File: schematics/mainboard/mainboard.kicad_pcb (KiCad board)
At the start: 4 copper layers, 92 x 166.8 mm, 75 parts, among them J1 SD_Card_Receptacle, J2 Conn_02x20_Odd_Even_MountingP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, J3 USB_C_Receptacle_USB2.0_16P, J6 Conn_01x12, P1 1-1473005-4, U1 AMS1117-3.3, U2 AMS1117-3.3, U3 MAX3421EETJ_T, U5 BQ24040DSQR, U6 TPS63002, U8 MAX9715xTE+, U9 AMS1117-3.3, Y1 12MHz

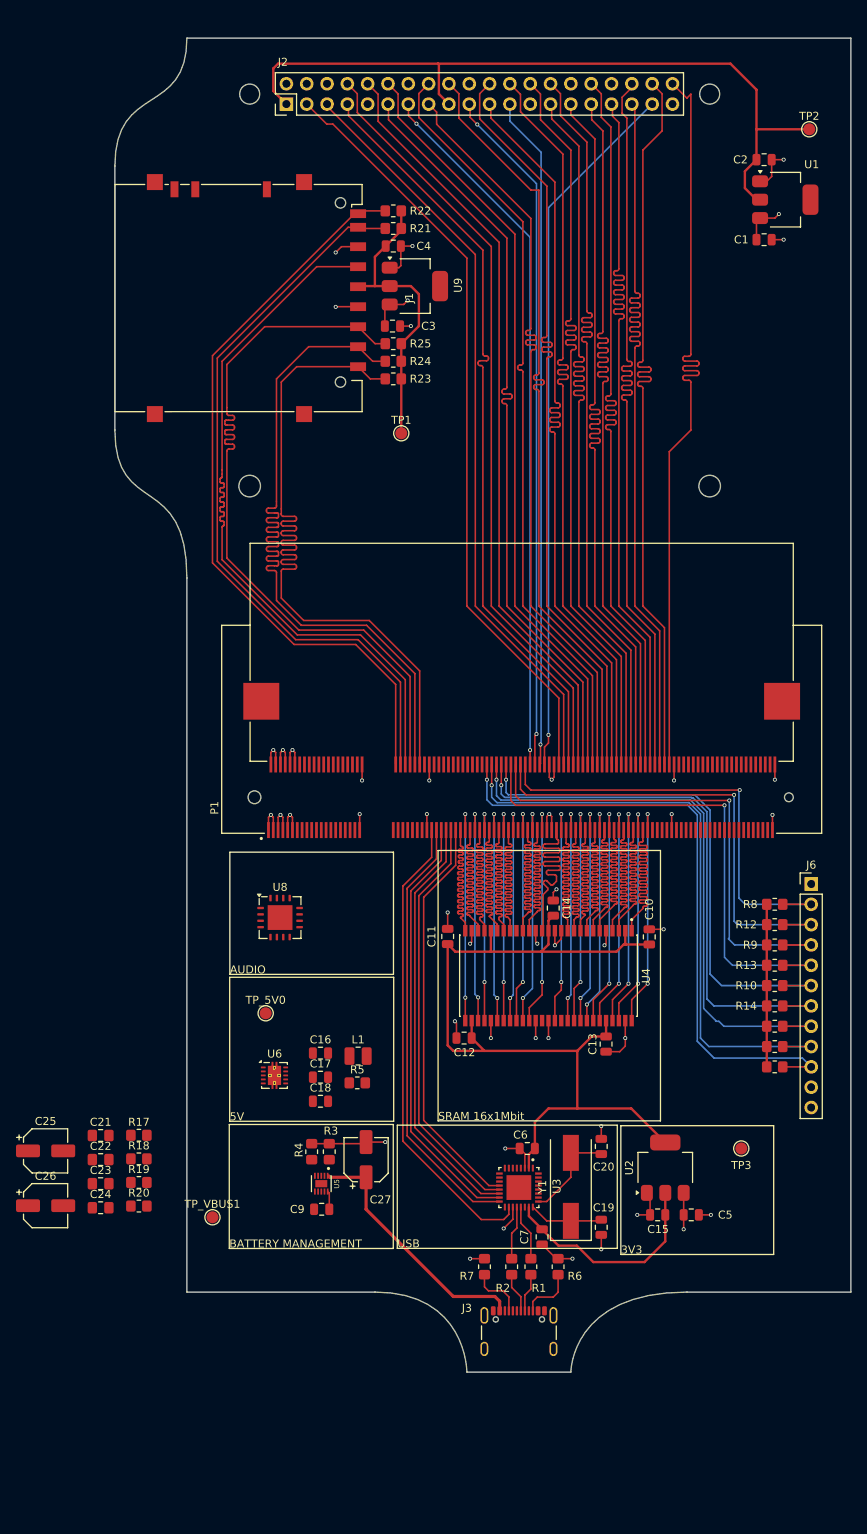
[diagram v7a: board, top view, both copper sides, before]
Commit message: Mainboard schematics, audio system and power traces.
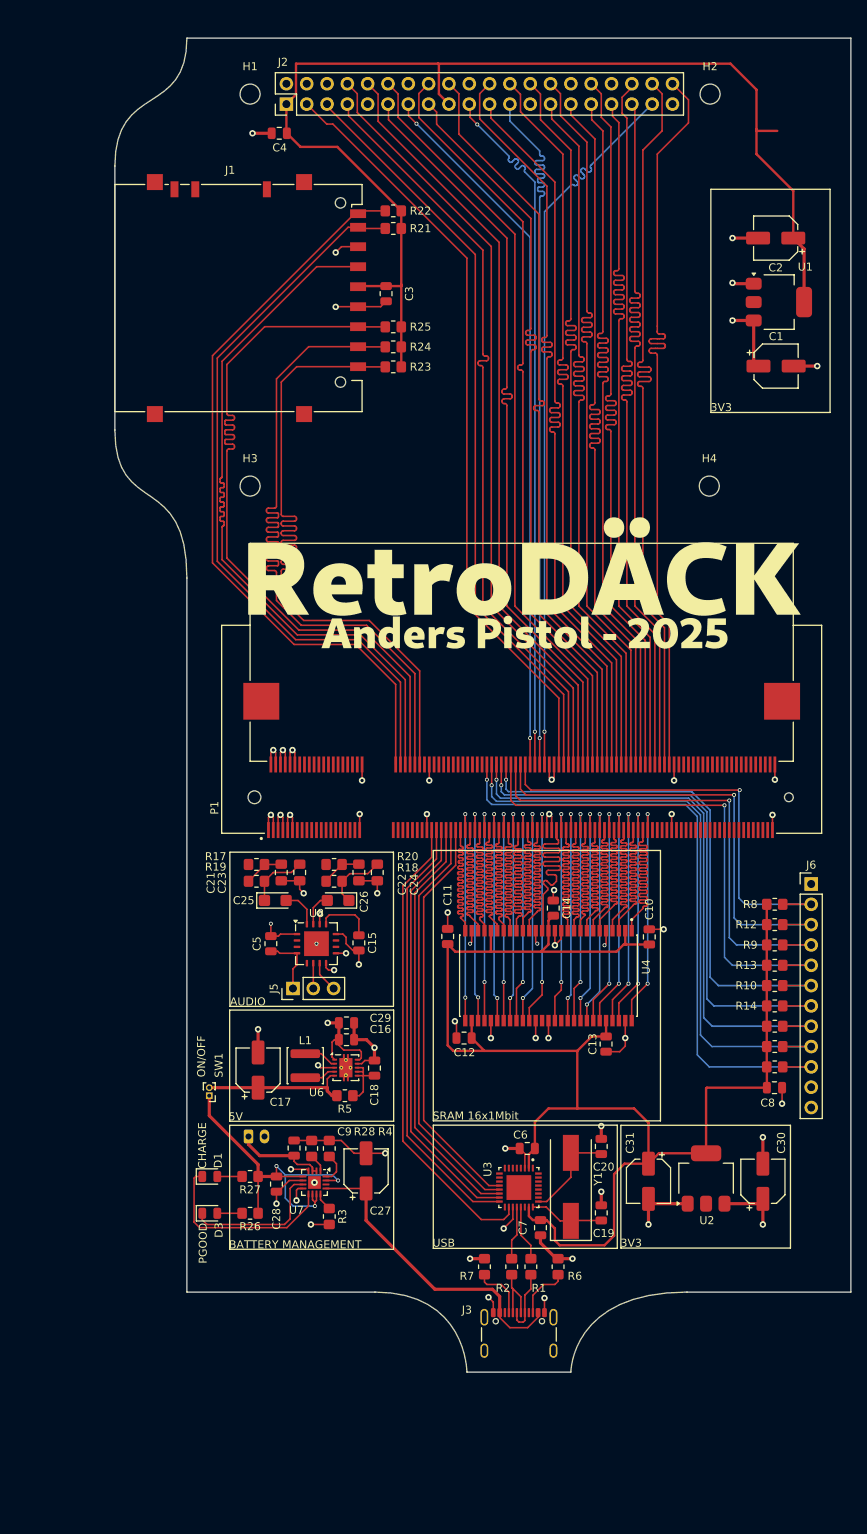
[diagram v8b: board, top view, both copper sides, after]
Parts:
- removed REF** (x2): MountingHole_2.7mm, MountingHole:MountingHole_2.7mm
- removed REF** (x2): MountingHole_2.5mm, MountingHole:MountingHole_2.5mm
- removed TP1: TP_3V3_SD, TestPoint:TestPoint_Pad_D1.5mm
- removed TP2: TP_3V3_LCD, TestPoint:TestPoint_Pad_D1.5mm
- removed TP3: TP_3V3, TestPoint:TestPoint_Pad_D1.5mm
- removed TP_5V0: TP_5V0, TestPoint:TestPoint_Pad_D1.5mm
- removed TP_VBUS1: TP_VBUS, TestPoint:TestPoint_Pad_D1.5mm
- removed U5: BQ24040DSQR, BQ24040DSQR:SON40P200X200X80-11N
- removed U9: AMS1117-3.3, Package_TO_SOT_SMD:SOT-223-3_TabPin2
- added C28: 10uF, Capacitor_SMD:C_0805_2012Metric, F.Cu at (126.2, 243.2)
- added C29: 10uF, Capacitor_SMD:C_0805_2012Metric, F.Cu at (134.9, 223.1)
- added C30: 10uF, Capacitor_SMD:CP_Elec_5x5.3, F.Cu at (187.0, 242.9)
- added C31: 22uF, Capacitor_SMD:CP_Elec_5x5.3, F.Cu at (172.7, 242.9)
- added C8: 1uF, Capacitor_SMD:C_0805_2012Metric, F.Cu at (188.4, 231.2)
- added D1: LED, LED_SMD:LED_0805_2012Metric, F.Cu at (117.9, 242.3)
- added D3: LED, LED_SMD:LED_0805_2012Metric, F.Cu at (117.9, 246.9)
- added H1: MountingHole, MountingHole:MountingHole_2.5mm, F.Cu at (122.9, 107.0)
- added H2: MountingHole, MountingHole:MountingHole_2.5mm, F.Cu at (180.4, 107.0)
- added H3: MountingHole, MountingHole:MountingHole_2.5mm, F.Cu at (122.9, 156.0)
- added H4: MountingHole, MountingHole:MountingHole_2.5mm, F.Cu at (180.3, 156.0)
- added J4: Conn_01x02, Connector_JST:JST_PH_S2B-PH-K_1x02_P2.00mm_Horizontal, B.Cu at (122.7, 237.3)
- added J5: Conn_01x03_Pin, Connector_PinHeader_2.54mm:PinHeader_1x03_P2.54mm_Vertical, F.Cu at (128.3, 218.8)
- added R26: 1k, Resistor_SMD:R_0805_2012Metric_Pad1.20x1.40mm_HandSolder, F.Cu at (122.9, 246.9)
- added R27: 1k, Resistor_SMD:R_0805_2012Metric_Pad1.20x1.40mm_HandSolder, F.Cu at (122.9, 242.3)
- added R28: 10k, Resistor_SMD:R_0805_2012Metric_Pad1.20x1.40mm_HandSolder, F.Cu at (130.6, 238.8)
- added SW1: SW_SPST, Connector_PinHeader_1.00mm:PinHeader_1x02_P1.00mm_Vertical, F.Cu at (117.8, 232.2)
- added U7: BQ24072RGT, Package_DFN_QFN:VQFN-16-1EP_3x3mm_P0.5mm_EP1.6x1.6mm, F.Cu at (130.9, 243.1)
- C1: value C -> 10uF; footprint Capacitor_SMD:C_0805_2012Metric -> Capacitor_SMD:CP_Elec_5x5.3
- C10, C11, C12, C13, C14, C15, C3, C4, C5, C6: value C -> 1uF
- C16: value 1u -> 10uF
- C17: value 10u -> 10uF; footprint Capacitor_SMD:C_0805_2012Metric -> Capacitor_SMD:CP_Elec_5x5.3
- C2: value C -> 22uF; footprint Capacitor_SMD:C_0805_2012Metric -> Capacitor_SMD:CP_Elec_5x5.3
- C25, C26: value 100uF -> 47uF; footprint Capacitor_SMD:CP_Elec_5x5.3 -> Capacitor_Tantalum_SMD:CP_EIA-3216-18_Kemet-A
- C7: value 1u -> 1uF
- C9: value 1u -> 4.7uF
- L1: value L -> 2.2uH; footprint Inductor_SMD:L_1008_2520Metric -> Inductor_SMD:L_APV_ANR4012
- R3: value 540 -> 1.18k
- R4: value 2k -> 1.13k
- moved C5 62.5 mm to (125.5, 213.2), turned to -90 degrees
- moved C24 54.3 mm to (138.8, 204.3), turned to 90 degrees
- moved C26 52.8 mm to (133.9, 207.8), turned to 180 degrees
- moved C15 50.5 mm to (136.5, 213.1), turned to -90 degrees
- moved C22 48.3 mm to (136.5, 204.3), turned to 90 degrees
- moved R20 47.4 mm to (133.4, 205.4)
- moved C23 46.2 mm to (129.1, 204.3), turned to -90 degrees
- moved R18 44.2 mm to (133.4, 203.3)
- moved C25 42.5 mm to (126.1, 207.8)
- moved R19 40.4 mm to (123.7, 205.4)
- moved C21 39.9 mm to (126.8, 204.3), turned to -90 degrees
- moved R17 36.9 mm to (123.7, 203.3)
- moved C4 20.0 mm to (126.5, 111.9), turned to 0 degrees
- moved C1 15.9 mm to (188.7, 141.0), turned to 0 degrees
- moved U1 12.8 mm to (189.0, 133.0)
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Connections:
- C1 pad 1: GND -> 5V0
- C1 pad 2: 5V0 -> GND
- C15 pad 1: GND -> Net-(U8-BIAS)
- C15 pad 2: 3V3 -> GND
- C17 pad 1: GND -> SYS_LOAD
- C17 pad 2: SYS_LOAD -> GND
- C2 pad 1: GND -> 3V3_LCD
- C2 pad 2: 3V3_LCD -> GND
- C21 pad 2: Net-(C21-Pad2) -> GND
- C22 pad 1: Net-(C21-Pad2) -> GND
- C23 pad 2: Net-(C21-Pad2) -> GND
- C24 pad 1: Net-(C21-Pad2) -> GND
- C3 pad 2: 5V0 -> 3V3_LCD
- C4 pad 2: 3V3_SD -> 3V3_LCD
- J1 pad 4: 3V3_SD -> 3V3_LCD
- R21 pad 2: 3V3_SD -> 3V3_LCD
- R22 pad 2: 3V3_SD -> 3V3_LCD
- R23 pad 2: 3V3_SD -> 3V3_LCD
- R24 pad 2: 3V3_SD -> 3V3_LCD
- R25 pad 2: 3V3_SD -> 3V3_LCD
- R3 pad 1: GND -> Net-(U7-ILIM)
- R3 pad 2: Net-(U5-ISET) -> GND
- R4 pad 1: GND -> Net-(U7-ISET)
- R4 pad 2: Net-(U5-PRETERM) -> GND
- U6 pad 10: unconnected-(U6-FB-Pad10) -> 5V0
- U8 pad 10: unconnected-(U8-OUTR--Pad10) -> Net-(U8-OUTR-)
- U8 pad 11: unconnected-(U8-OUTR+-Pad11) -> Net-(U8-OUTR+)
- U8 pad 13: unconnected-(U8-BIAS-Pad13) -> Net-(U8-BIAS)
- U8 pad 2: unconnected-(U8-OUTL+-Pad2) -> Net-(U8-OUTL+)
- U8 pad 3: unconnected-(U8-OUTL--Pad3) -> Net-(U8-OUTL-)
- U8 pad 6: unconnected-(U8-GAIN-Pad6) -> Net-(J5-Pin_2)
- U8 pad 8: unconnected-(U8-~{SHDN}-Pad8) -> 5V0
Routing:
- net GND: track 117.7 -> 183.4 mm, vias 40 -> 56
- net 3V3_LCD: track 94.7 -> 148.5 mm
- net Net-(SW1-A): track 0.00 -> 43.8 mm, vias 0 -> 3
- net 3V3_SD: track 37.1 -> 0.00 mm
- net SRAM_A17: track 0.00 -> 29.6 mm
- net 3V3: track 155.4 -> 183.0 mm
- net 5V0: track 26.9 -> 52.7 mm, vias 6 -> 9
- net Net-(D1-K): track 0.00 -> 23.8 mm
- net SYS_LOAD: track 0.00 -> 18.8 mm
- net Net-(D3-K): track 0.00 -> 17.9 mm
- net BAT+: track 2.29 -> 11.5 mm
- net Net-(U6-EN): track 0.00 -> 8.23 mm
- net Net-(C24-Pad2): track 0.00 -> 8.04 mm
- net Net-(C23-Pad1): track 0.00 -> 7.69 mm
- net LCD_TOUCH_CLK: track 84.2 -> 91.6 mm
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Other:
- board text added: "CHARGE"
- board text added: "ON/OFF"
- board text added: "PGOOD"
